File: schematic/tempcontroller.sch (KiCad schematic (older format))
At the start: 3 parts

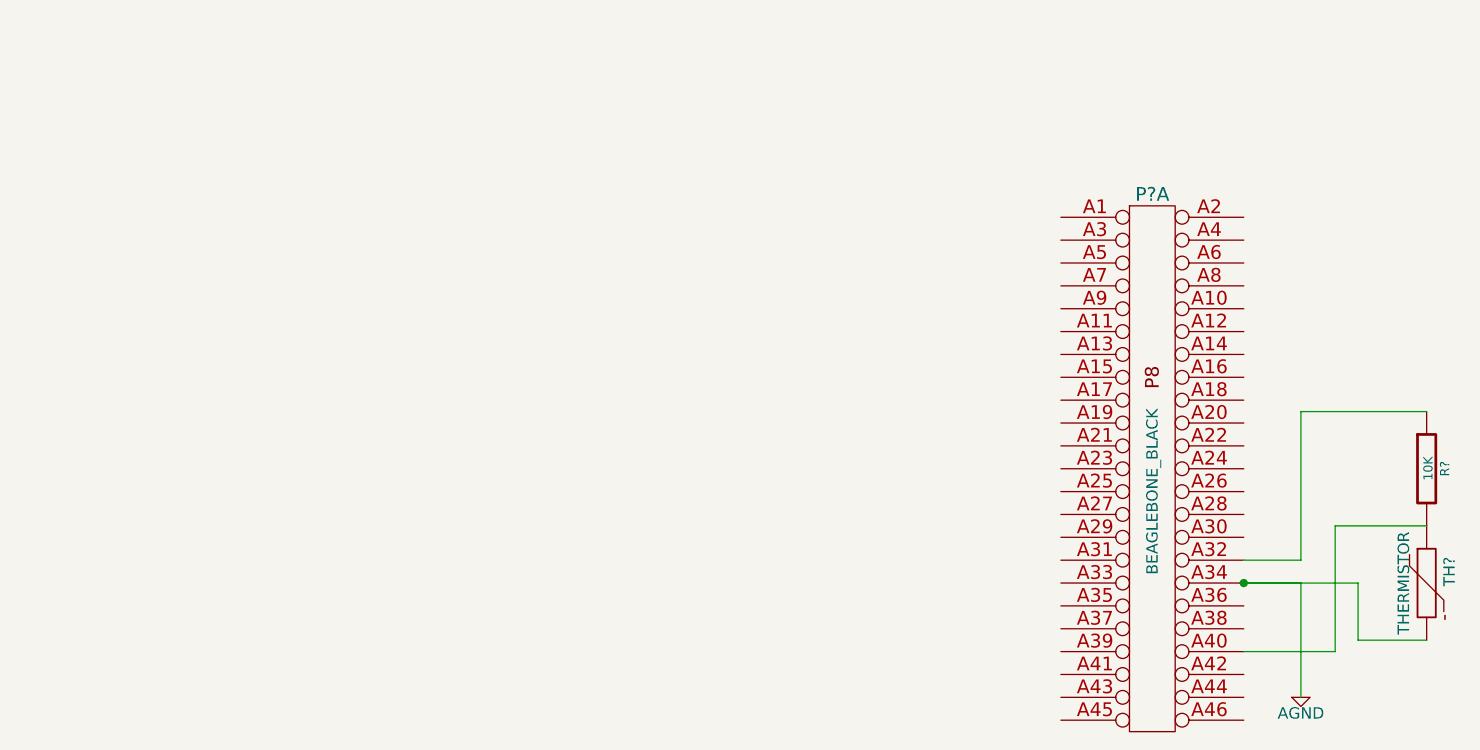
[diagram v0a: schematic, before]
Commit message: Updated Schematic to use DS18B20 temp sensor
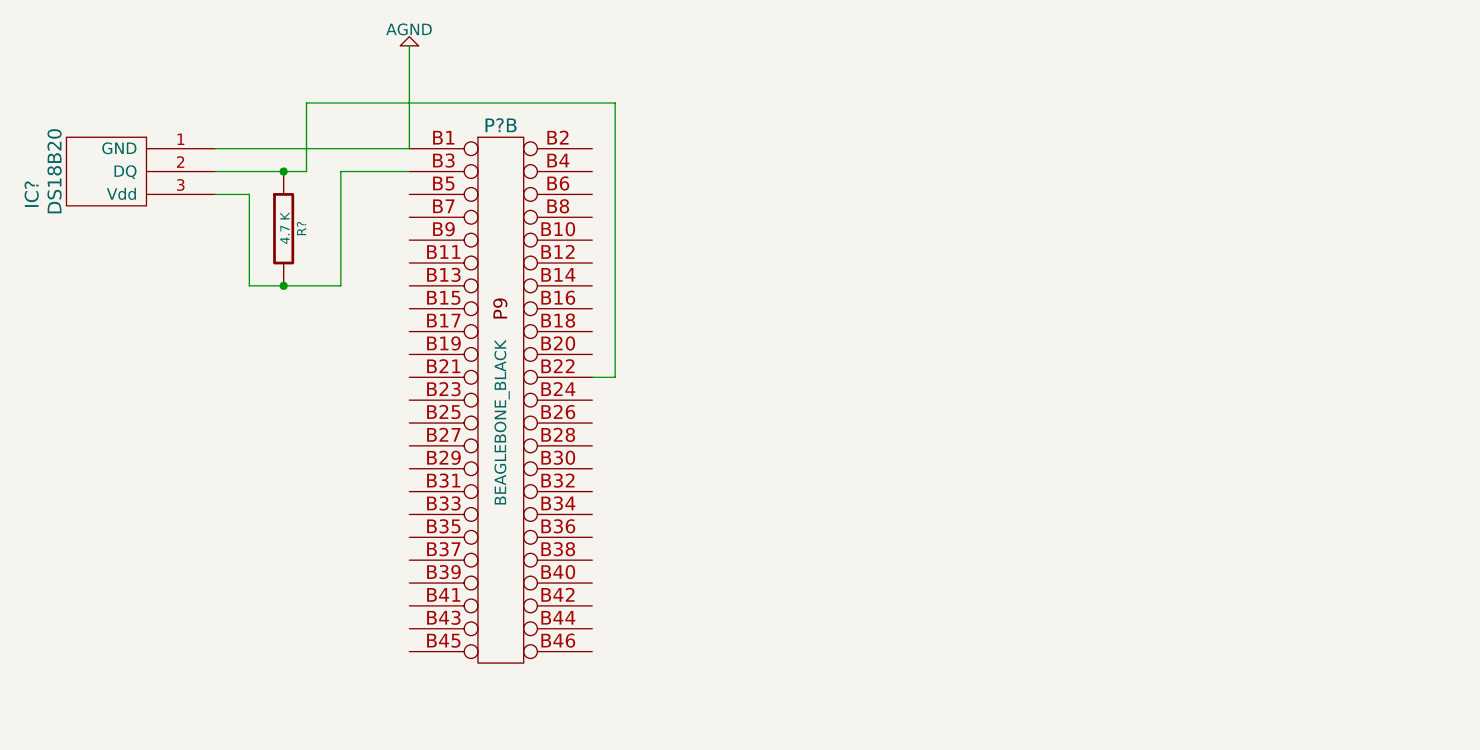
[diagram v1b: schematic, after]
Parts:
- removed P?: BEAGLEBONE_BLACK, ~, symbol BEAGLEBONE_BLACK
- removed R?: 10K, ~, symbol R
- removed TH?: THERMISTOR, ~, symbol THERMISTOR
- added IC?: DS18B20, ~, symbol DS18B20
- added P?: BEAGLEBONE_BLACK, ~, symbol BEAGLEBONE_BLACK
- added R?: 4.7 K, ~, symbol R
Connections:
- net AGND: now also IC?.1 (GND), P?.B1 (GND)
- new net: IC?.2 (DQ), P?.B22 (P22), R?.1
- new net: IC?.3 (Vdd), P?.B3, R?.2
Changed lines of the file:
@@
 EESchema Schematic File Version 2
+LIBS:TempController
 LIBS:power
 LIBS:device
@@
 LIBS:beagleboard
 LIBS:tempcontroller-cache
+LIBS:tempcontroller-cache
 EELAYER 27 0
 EELAYER END
@@
 Sheet 1 1
 Title "noname.sch"
-Date "6 jun 2014"
+Date "8 feb 2015"
 Rev ""
 Comp ""
@@
 $EndDescr
 $Comp
-L THERMISTOR TH?
-U 1 1 538D4838
-P 7550 3950
-F 0 "TH?" V 7650 4000 50  0000 C CNN
-F 1 "THERMISTOR" V 7450 3950 50  0000 C CNN
-F 2 "~" H 7550 3950 60  0000 C CNN
-F 3 "~" H 7550 3950 60  0000 C CNN
-	1    7550 3950
+L DS18B20 IC?
+U 1 1 54D6B80B
+P 1850 2150
+F 0 "IC?" H 1750 2550 60  0000 C CNN
+F 1 "DS18B20" H 1850 2450 60  0000 C CNN
+F 2 "~" H 1850 2150 60  0000 C CNN
+F 3 "~" H 1850 2150 60  0000 C CNN
+	1    1850 2150
+	0    -1   -1   0
+$EndComp
+$Comp
+L BEAGLEBONE_BLACK P?
+U 2 1 54D71F34
+P 3500 3250
+F 0 "P?" H 3500 4550 60  0000 C CNN
+F 1 "BEAGLEBONE_BLACK" V 3500 3250 50  0000 C CNN
+F 2 "~" H 3500 3250 60  0000 C CNN
+F 3 "~" H 3500 3250 60  0000 C CNN
+	2    3500 3250
 	1    0    0    -1
 $EndComp
 $Comp
 L R R?
-U 1 1 538D484C
-P 7550 3450
-F 0 "R?" V 7630 3450 40  0000 C CNN
-F 1 "10K" V 7557 3451 40  0000 C CNN
-F 2 "~" V 7480 3450 30  0000 C CNN
-F 3 "~" H 7550 3450 30  0000 C CNN
-	1    7550 3450
-	1    0    0    -1
-$EndComp
-$Comp
-L BEAGLEBONE_BLACK P?
-U 1 1 538D4F55
-P 6350 3550
-F 0 "P?" H 6350 4850 60  0000 C CNN
-F 1 "BEAGLEBONE_BLACK" V 6350 3550 50  0000 C CNN
-F 2 "~" H 6350 3550 60  0000 C CNN
-F 3 "~" H 6350 3550 60  0000 C CNN
-	1    6350 3550
+U 1 1 54D79215
+P 2550 2400
+F 0 "R?" V 2630 2400 40  0000 C CNN
+F 1 "4.7 K" V 2557 2401 40  0000 C CNN
+F 2 "~" V 2480 2400 30  0000 C CNN
+F 3 "~" H 2550 2400 30  0000 C CNN
+	1    2550 2400
 	1    0    0    -1
 $EndComp
 Wire Wire Line
-	6750 3850 7000 3850
+	2250 2150 2550 2150
 Wire Wire Line
-	7000 3850 7000 3200
+	2550 2150 2650 2150
 Wire Wire Line
-	7000 3200 7550 3200
+	2650 2150 2650 1850
 Wire Wire Line
-	7550 4200 7250 4200
+	2650 1850 4000 1850
 Wire Wire Line
-	7250 4200 7250 3950
+	4000 1850 4000 3050
 Wire Wire Line
-	7250 3950 6750 3950
+	4000 3050 3900 3050
+Connection ~ 2550 2150
 Wire Wire Line
-	6750 4250 7150 4250
+	2250 2250 2400 2250
 Wire Wire Line
-	7150 4250 7150 3700
+	2400 2250 2400 2650
 Wire Wire Line
-	7150 3700 7550 3700
+	2400 2650 2550 2650
+Wire Wire Line
+	2550 2650 2800 2650
+Wire Wire Line
+	2800 2650 2800 2150
+Wire Wire Line
+	2800 2150 3100 2150
+Connection ~ 2550 2650
+Wire Wire Line
+	2250 2050 3100 2050
 $Comp
 L AGND #PWR?
-U 1 1 538D514D
-P 7000 4450
-F 0 "#PWR?" H 7000 4450 40  0001 C CNN
-F 1 "AGND" H 7000 4380 50  0000 C CNN
-F 2 "" H 7000 4450 60  0000 C CNN
-F 3 "" H 7000 4450 60  0000 C CNN
-	1    7000 4450
-	1    0    0    -1
+U 1 1 54D79309
+P 3100 1600
+F 0 "#PWR?" H 3100 1600 40  0001 C CNN
+F 1 "AGND" H 3100 1530 50  0000 C CNN
+F 2 "~" H 3100 1600 60  0000 C CNN
+F 3 "~" H 3100 1600 60  0000 C CNN
+	1    3100 1600
+	-1   0    0    1
 $EndComp
 Wire Wire Line
-	6750 3950 6750 3950
-Wire Wire Line
-	6750 3950 7000 3950
-Wire Wire Line
-	7000 3950 7000 4450
-Connection ~ 6750 3950
+	3100 2050 3100 1600
 $EndSCHEMATC
